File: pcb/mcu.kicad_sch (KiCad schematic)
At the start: 22 parts, among them SW1 GSPTS0018, SW2 GSPTS0018, U1 STM32H730VBTx, Y1 ECS-160-12-33B2Q-JES-TR3

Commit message: Finished user interface
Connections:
- net MODE_1: now also U1.16 (PC1)
- net MODE_2: now also U1.17 (PC2_C)
- net MODE_4: now also U1.18 (PC3_C)
- net MODE_C: now also U1.15 (PC0)
- net BTN_0: now reaches U1.2 (PE3)
- net BATT_SENSE: now reaches U1.22 (PA0)
- net BTN_1: now reaches U1.3 (PE4)
- net BTN_2: now reaches U1.4 (PE5)
- net BTN_3: now reaches U1.5 (PE6)

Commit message: Start layout
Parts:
- C1: renamed from C14; footprint (none) -> Capacitor_SMD:C_0603_1608Metric
- C10: renamed from C9; footprint (none) -> Capacitor_SMD:C_0603_1608Metric
- C11: renamed from C10; footprint (none) -> Capacitor_SMD:C_0603_1608Metric
- C12: renamed from C6; footprint (none) -> Capacitor_SMD:C_0603_1608Metric
- C14: renamed from C11; footprint (none) -> Capacitor_SMD:C_0603_1608Metric
- C15: renamed from C5; footprint (none) -> Capacitor_SMD:C_0603_1608Metric
- C2: renamed from C13; footprint (none) -> Capacitor_SMD:C_0603_1608Metric
- C3: renamed from C12; footprint (none) -> Capacitor_SMD:C_0603_1608Metric
- C5: renamed from C7; footprint (none) -> Capacitor_SMD:C_0603_1608Metric
- C6: renamed from C2; footprint (none) -> Capacitor_SMD:C_0603_1608Metric
- C7: renamed from C8; footprint (none) -> Capacitor_SMD:C_0603_1608Metric
- C8: renamed from C1; footprint (none) -> Capacitor_SMD:C_0603_1608Metric
- R1: renamed from R2; footprint (none) -> Resistor_SMD:R_0603_1608Metric
- renumbered C15 to C13, C3 to C4, C4 to C9, FB2 to FB1, R1 to R2
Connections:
- net BTN_0: now also U1.81 (PD0); no longer U1.2 (PE3)
- net BTN_1: now also U1.82 (PD1); no longer U1.3 (PE4)
- net BTN_2: now also U1.83 (PD2); no longer U1.4 (PE5)
- net BTN_3: now also U1.84 (PD3); no longer U1.5 (PE6)
- net MODE_1: now also U1.86 (PD5); no longer U1.16 (PC1)
- net MODE_2: now also U1.87 (PD6); no longer U1.17 (PC2_C)
- net MODE_4: now also U1.88 (PD7); no longer U1.18 (PC3_C)
- net MODE_C: now also U1.85 (PD4); no longer U1.15 (PC0)
- net I2C1_SCL: now reaches U1.92 (PB6)
- net I2C1_SDA: now reaches U1.93 (PB7)
- net BATT_SENSE: no longer names the net of U1.22 (PA0)
- new net BATT_ISENSE: U1.16 (PC1)
- new net BATT_VSENSE: U1.15 (PC0)

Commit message: Layout power
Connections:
- net USB_DM renamed USB_D-
- net USB_DP renamed USB_D+

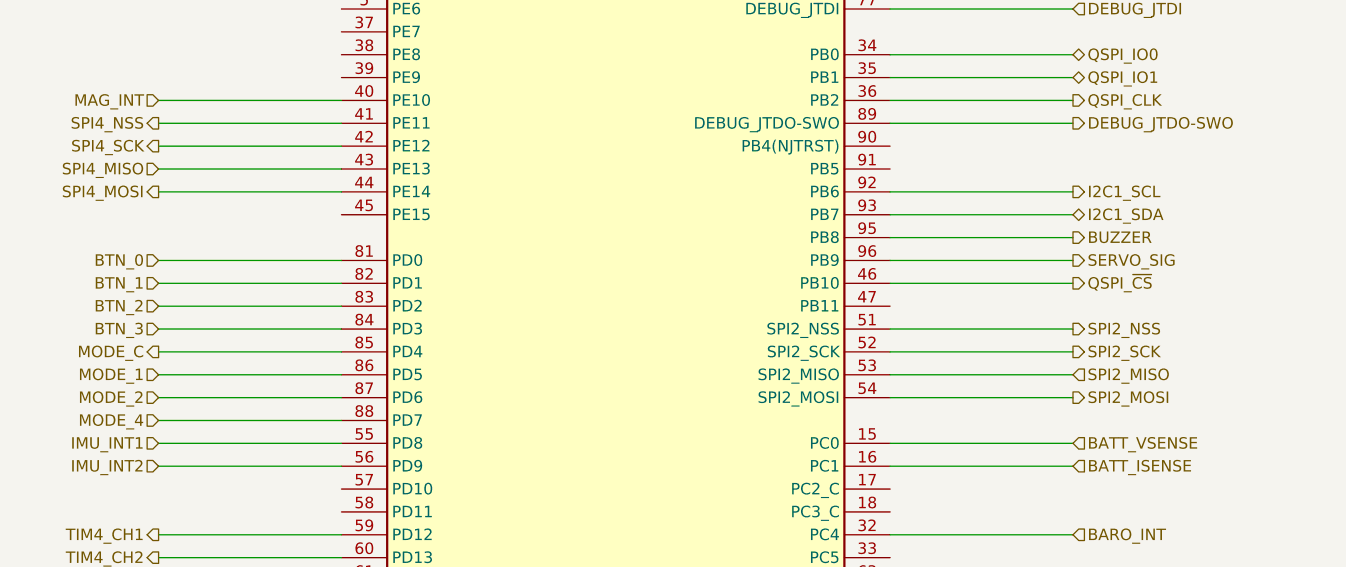
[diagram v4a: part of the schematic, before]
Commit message: Finish routing with rotated STM32
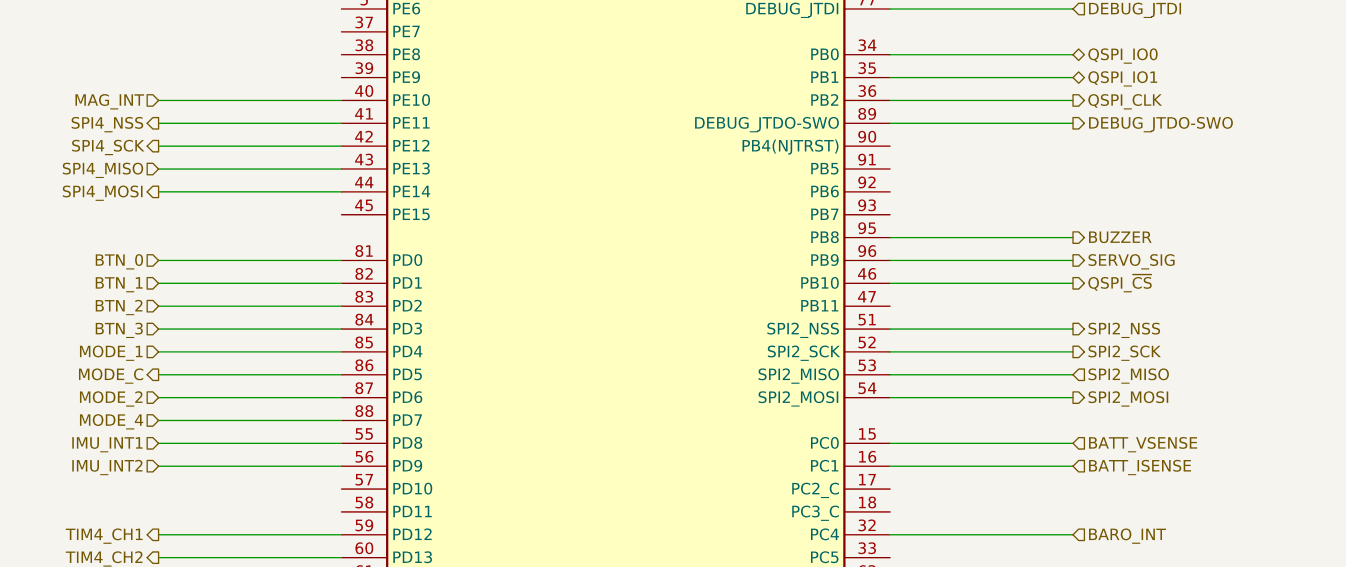
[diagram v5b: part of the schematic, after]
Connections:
- net MODE_1: now also U1.85 (PD4); no longer U1.86 (PD5)
- net MODE_C: now also U1.86 (PD5); no longer U1.85 (PD4)
- net I2C1_SCL: no longer names the net of U1.92 (PB6)
- net I2C1_SDA: no longer names the net of U1.93 (PB7)

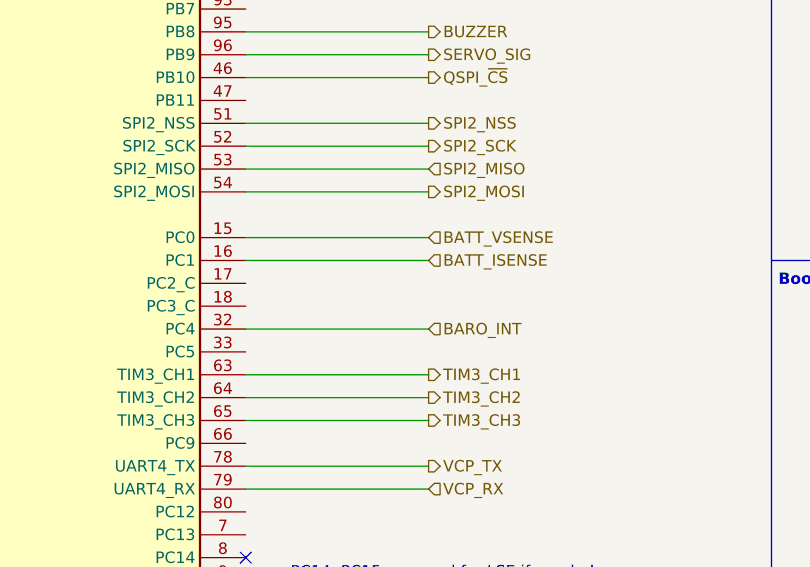
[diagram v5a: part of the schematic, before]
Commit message: Incorporate feedback servo with 4 pin molex and additional ADC channel
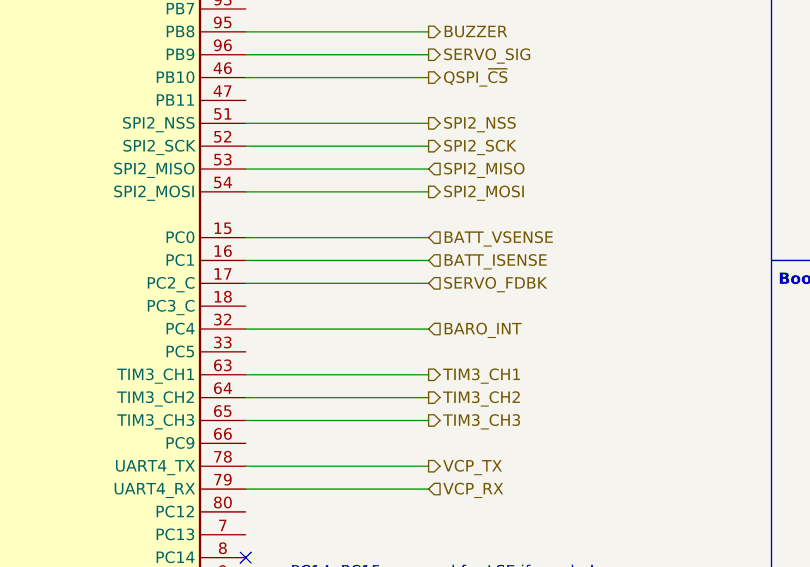
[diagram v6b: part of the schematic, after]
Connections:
- net SERVO_FDBK: now reaches U1.17 (PC2_C)

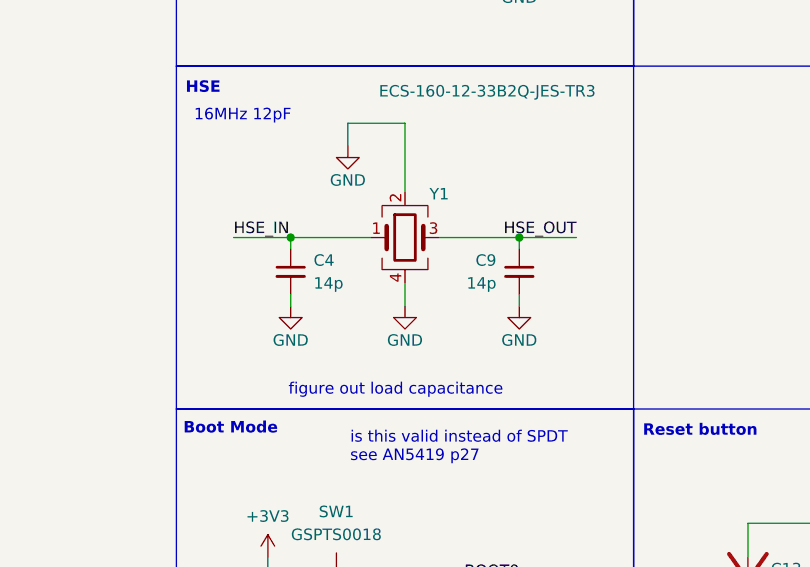
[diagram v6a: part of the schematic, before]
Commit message: Add buck converter inductor 3D model
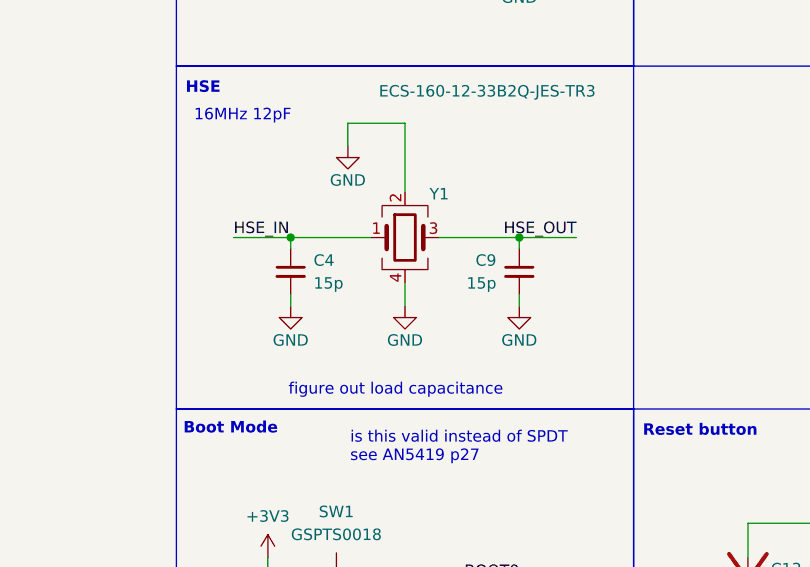
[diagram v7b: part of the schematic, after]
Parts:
- C4, C9: value 14p -> 15p

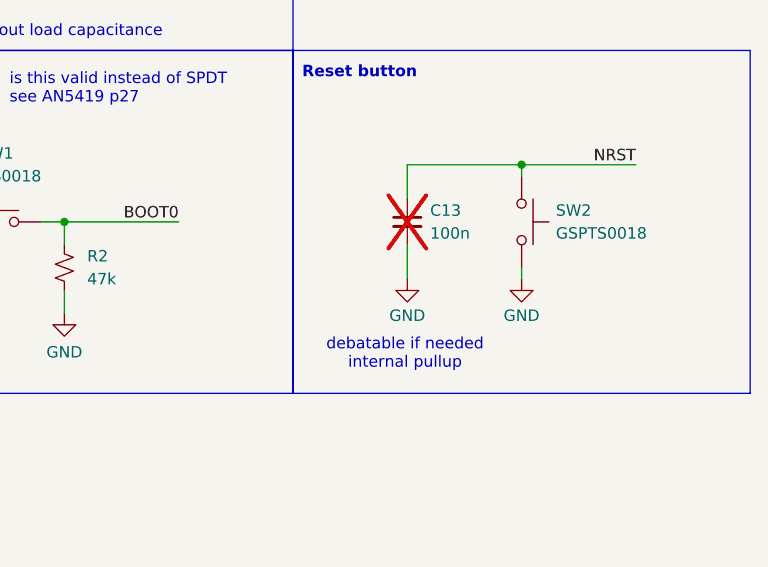
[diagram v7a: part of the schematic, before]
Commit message: Disable DNP for NRST capacitor
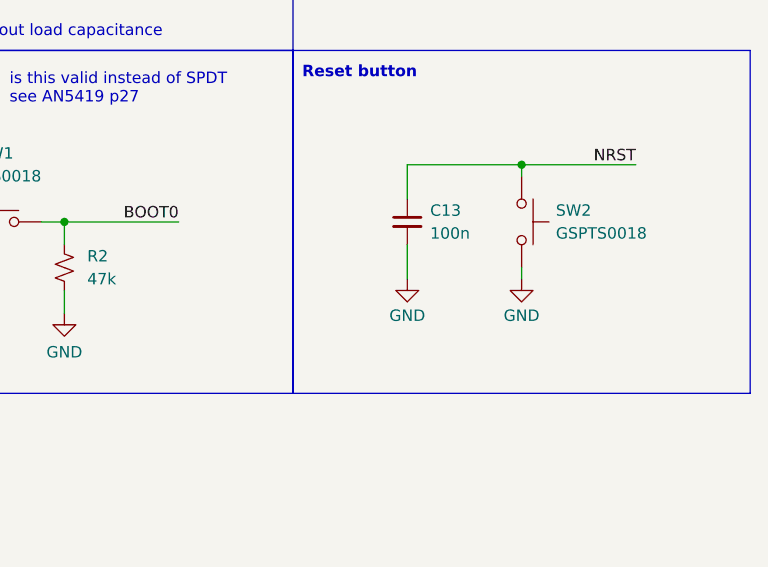
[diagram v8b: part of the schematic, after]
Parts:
- C13: now fitted
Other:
- note removed: "debatable if needed internal pullup"
